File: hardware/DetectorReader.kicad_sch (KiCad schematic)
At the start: 17 parts, among them J1 10118194-0001LF, J2 Combo_Conn, J4 SMA_Conn, SW1 SeqTrig_SW, U1 ATtiny814-SS, U2 FT231XS-R, U3 XC0900P-10S

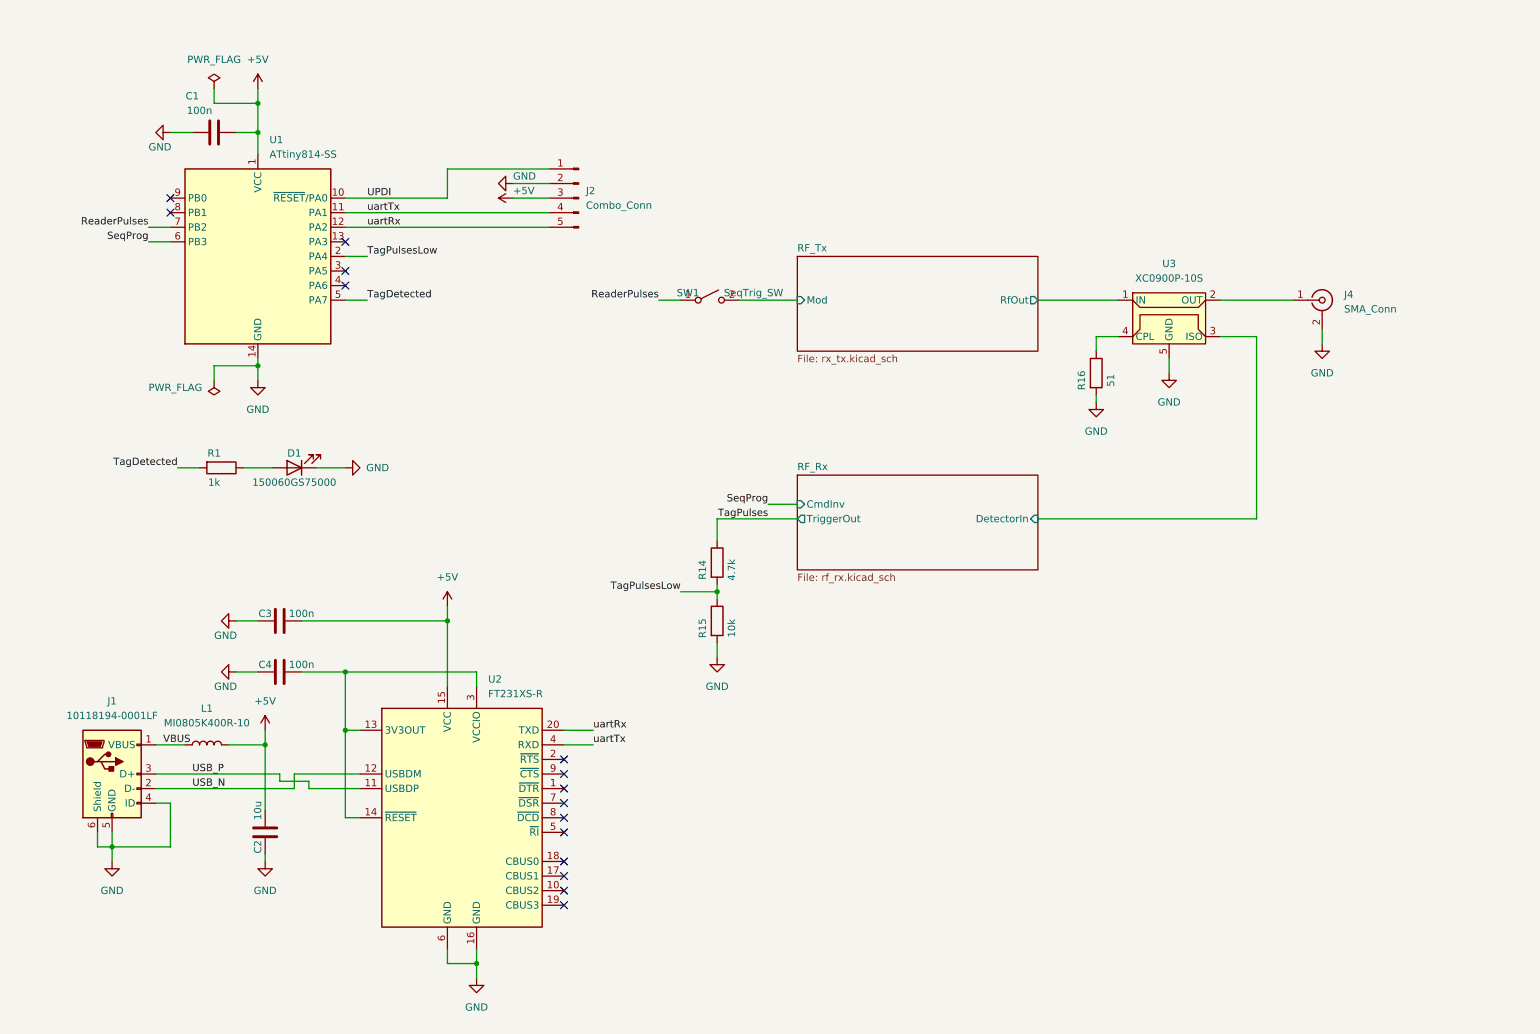
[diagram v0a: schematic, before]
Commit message: splitted quad opamp into dual opamp and comparator for better digitalization and smaller board
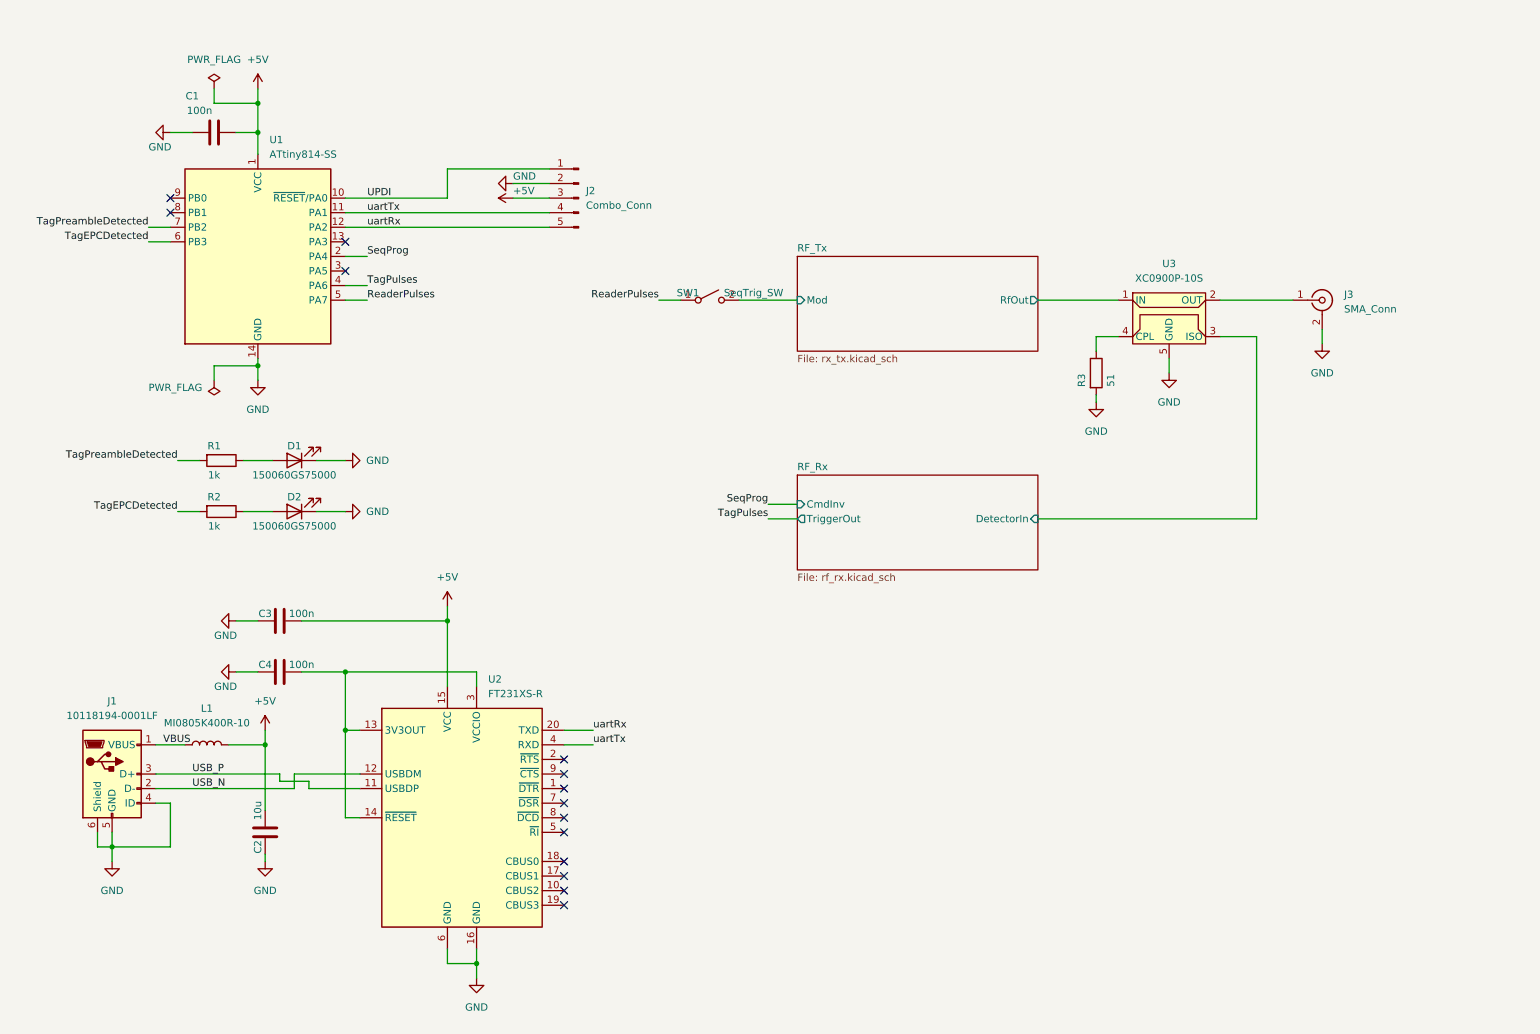
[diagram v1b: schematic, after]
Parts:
- removed R14: 4.7k, Resistor_SMD:R_0603_1608Metric, symbol Device:R
- removed R15: 10k, Resistor_SMD:R_0603_1608Metric, symbol Device:R
- added D1: 150060GS75000, LED_SMD:LED_0603_1608Metric, symbol Device:LED
- added R1: 1k, Resistor_SMD:R_0603_1608Metric, symbol Device:R
- renumbered D1 to D2, J4 to J3, R1 to R2, R16 to R3
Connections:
- net TagPulsesLow is gone; now on net SeqProg: U1.2 (PA4)
- net GND: now also D1.1 (K)
- net ReaderPulses: now also U1.5 (PA7); no longer U1.7 (PB2)
- net SeqProg: no longer U1.6 (PB3)
- net TagPulses: now also U1.4 (PA6)
- net TagDetected renamed TagEPCDetected
- net TagEPCDetected: now also U1.6 (PB3); no longer U1.5 (PA7)
- new net: D1.2 (A), R1.1
- new net TagPreambleDetected: R1.2, U1.7 (PB2)
- no-connect marks 15 -> 14
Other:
- moved on the sheet: D2, R2

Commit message: Updated schematic, PCB and fabrication files
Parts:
- added C3, C6, C7: 22u, Capacitor_SMD:C_0603_1608Metric, symbol Device:C
- added L2, L3: MI0805K400R-10, Inductor_SMD:L_0805_2012Metric, symbol Device:L
- C2: value 10u -> 22u
- D1: value 150060GS75000 -> 150060RS75000
- renumbered C3 to C4, C4 to C5
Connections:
- net +5V: now also C3.2, L2.1, L3.1; no longer C1.2, U1.1 (VCC)
- net GND: now also C3.1, C6.1, C7.1
- new net +5VAnalog: C7.2, L3.2
- new net +5VDigital: C1.2, C6.2, L2.2, U1.1 (VCC)
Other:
- moved on the sheet: C2, C4, C5, U2

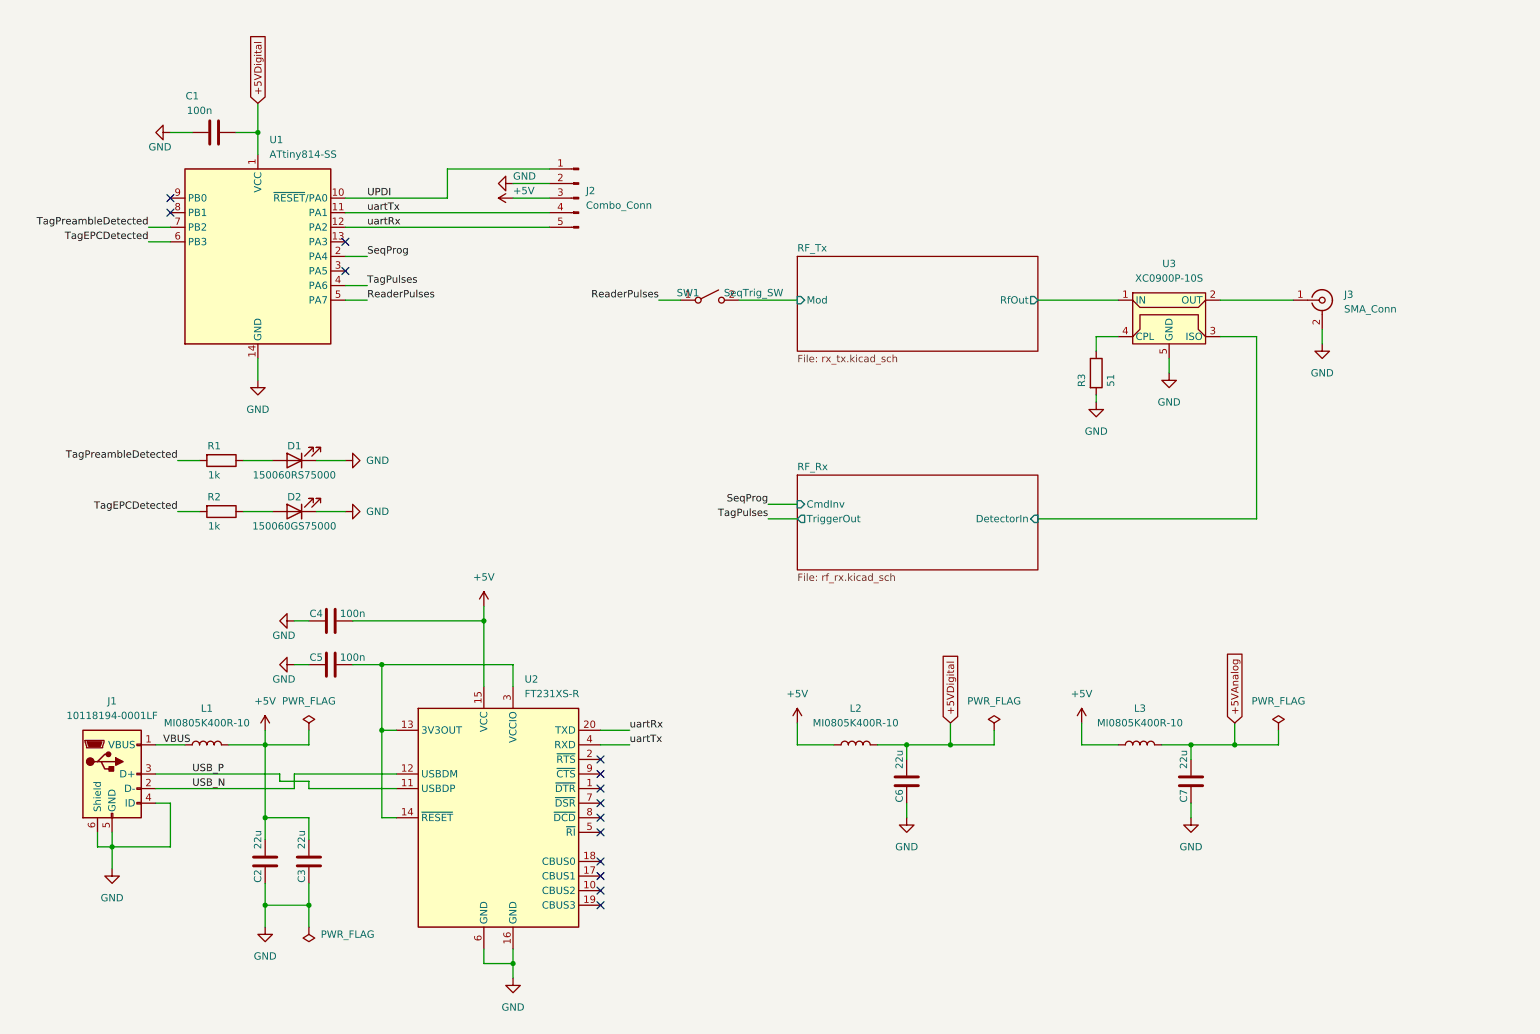
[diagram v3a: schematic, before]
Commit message: Rev 2. Using USB-C, configurable Tx, op-amp based LF amplifier, tri-color indicator. Using platformIO for firmware, splitted code into separate files.
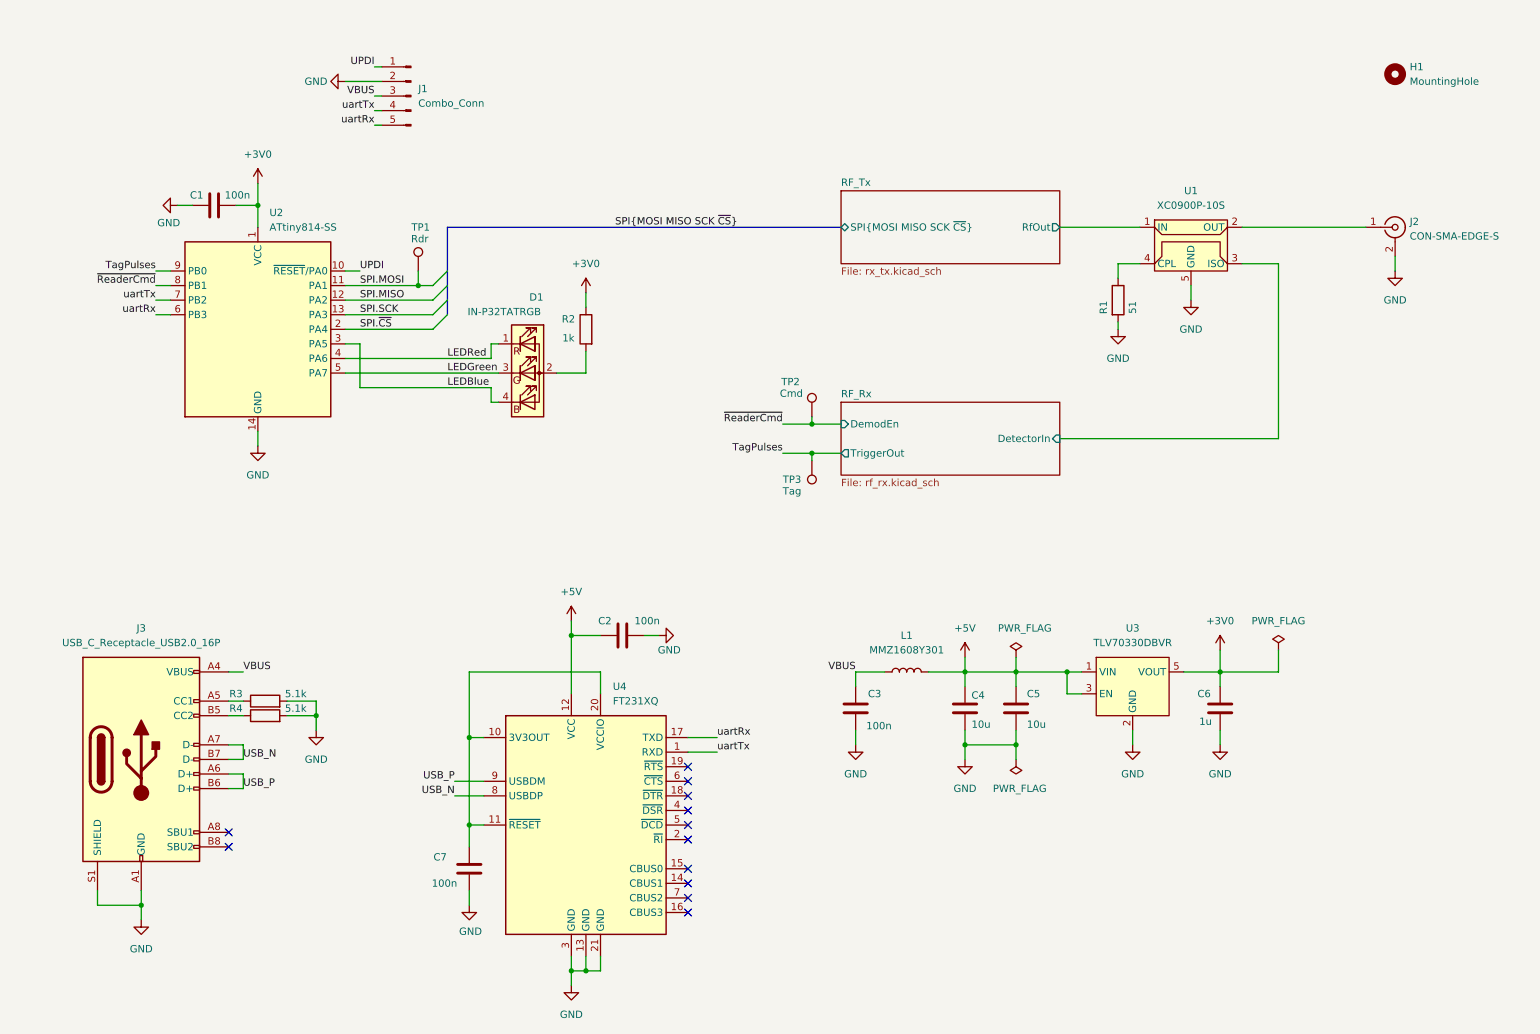
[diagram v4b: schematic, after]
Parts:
- removed C7: 22u, Capacitor_SMD:C_0603_1608Metric, symbol Device:C
- removed D1: 150060RS75000, LED_SMD:LED_0603_1608Metric, symbol Device:LED
- removed D2: 150060GS75000, LED_SMD:LED_0603_1608Metric, symbol Device:LED
- removed J1: 10118194-0001LF, Connector_USB:USB_Micro-B_Amphenol_10118194_Horizontal, symbol Connector:USB_B_Micro
- removed J2: Combo_Conn, Connector_PinHeader_2.54mm:PinHeader_1x05_P2.54mm_Vertical, symbol Connector:Conn_01x05_Male
- removed L2, L3: MI0805K400R-10, Inductor_SMD:L_0805_2012Metric, symbol Device:L
- removed R2: 1k, Resistor_SMD:R_0603_1608Metric, symbol Device:R
- removed SW1: SeqTrig_SW, Connector_PinHeader_2.54mm:PinHeader_1x02_P2.54mm_Vertical, symbol Switch:SW_SPST
- removed U2: FT231XS-R, Package_SO:SSOP-20_3.9x8.7mm_P0.635mm, symbol Interface_USB:FT231XS
- added C3: 100n, Capacitor_SMD:C_0603_1608Metric, symbol Device:C
- added D1: IN-P32TATRGB, ProjLib:LED_SMD_IN-P32TATRGB, symbol Device:LED_RAGB
- added H1: MountingHole, MountingHole:MountingHole_3.2mm_M3_DIN965, symbol Mechanical:MountingHole
- added J1: Combo_Conn, Connector_PinHeader_2.54mm:PinHeader_1x05_P2.54mm_Vertical, symbol Connector:Conn_01x05_Pin
- added J3: USB_C_Receptacle_USB2.0_16P, Connector_USB:USB_C_Receptacle_GCT_USB4105-xx-A_16P_TopMnt_Horizontal, symbol Connector:USB_C_Receptacle_USB2.0_16P
- added R3, R4: 5.1k, Resistor_SMD:R_0603_1608Metric, symbol Device:R
- added TP1: Rdr, ProjLib:Single_Pin, symbol Connector:TestPoint
- added TP2: Cmd, ProjLib:Single_Pin, symbol Connector:TestPoint
- added TP3: Tag, ProjLib:Single_Pin, symbol Connector:TestPoint
- added U3: TLV70330DBVR, Package_TO_SOT_SMD:SOT-23-5, symbol ProjLib:TLV70330
- added U4: FT231XQ, Package_DFN_QFN:QFN-20-1EP_4x4mm_P0.5mm_EP2.5x2.5mm, symbol Interface_USB:FT231XQ
- C4: renamed from C2; value 22u -> 10u
- C5: renamed from C3; value 22u -> 10u
- C6: value 22u -> 1u
- J2: renamed from J3; value SMA_Conn -> CON-SMA-EDGE-S; footprint Connector_Coaxial:SMA_Samtec_SMA-J-P-X-ST-EM1_EdgeMount -> Connector_Coaxial:SMA_Samtec_SMA-J-P-H-ST-EM1_EdgeMount
- L1: value MI0805K400R-10 -> MMZ1608Y301; footprint Inductor_SMD:L_0805_2012Metric -> Inductor_SMD:L_0603_1608Metric
- renumbered C4 to C2, C5 to C7, R3 to R1, R1 to R2, U3 to U1, U1 to U2
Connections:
- net +5VDigital is gone; now on net +3V0: C1.2, C6.2, U2.1 (VCC)
- net TagEPCDetected is gone; now on net uartRx: U2.6 (PB3)
- net +5V: now also U3.1 (VIN), U3.3 (EN), U4.12 (VCC)
- net GND: now also C3.1, J1.2 (Pin_2), J3.A1 (GND), J3.A12 (GND), J3.B1 (GND), J3.B12 (GND), J3.S1 (SHIELD), R3.2, R4.2, U3.2 (GND), U4.13 (GND), U4.21 (GND), U4.3 (GND)
- net TagPulses: now also U2.9 (PB0), TP3.1; no longer U2.4 (PA6)
- net UPDI: now also J1.1 (Pin_1)
- net USB_N: now also J3.A7 (D-), J3.B7 (D-), U4.8 (USBDP)
- net USB_P: now also J3.A6 (D+), J3.B6 (D+), U4.9 (USBDM)
- net VBUS: now also C3.2, J1.3 (Pin_3), J3.A4 (VBUS), J3.A9 (VBUS), J3.B4 (VBUS), J3.B9 (VBUS)
- net uartRx: now also J1.5 (Pin_5), U4.17 (TXD); no longer U2.12 (PA2)
- net uartTx: now also U2.7 (PB2), J1.4 (Pin_4), U4.1 (RXD); no longer U2.11 (PA1)
- net at C7.2: now also U4.10 (3V3OUT), U4.11 (~{RESET}), U4.20 (VCCIO)
- net +3V0: now reaches R2.1
- net +3V0: now also U3.5 (VOUT)
- net SPI.SCK: now reaches U2.13 (PA3)
- net LEDBlue: now reaches U2.3 (PA5)
- net LEDBlue: now also D1.4 (BK)
- net ~{ReaderCmd}: now reaches U2.8 (PB1)
- net ~{ReaderCmd}: now also TP2.1
- net ReaderPulses renamed LEDGreen
- net LEDGreen: now also D1.3 (GK)
- net SeqProg renamed SPI.~{CS}
- net TagPreambleDetected: no longer names the net of R2.2
- net TagPreambleDetected: now also D1.2 (A); no longer U2.7 (PB2)
- new net: J3.A5 (CC1), R3.1
- new net: J3.B5 (CC2), R4.1
- new net LEDRed: D1.1 (RK), U2.4 (PA6)
- new net SPI.MISO: U2.12 (PA2)
- new net SPI.MOSI: TP1.1, U2.11 (PA1)
- no-connect marks 14 -> 12
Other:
- sheet RF_Rx ports: added DemodEn; removed CmdInv
- sheet RF_Tx ports: added SPI{MOSI MISO SCK ~{CS}}; removed Mod
- moved on the sheet: C1, C2, C4, C5, C7, J2, L1, R1, R2, U1, U2

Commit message: Rev 3. Back to transistor-based design since op-amp approach did not work well. Using UART bridge from other brand as FTDI was sold out.
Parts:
- removed C3, C7: 100n, Capacitor_SMD:C_0603_1608Metric, symbol Device:C
- removed L1: MMZ1608Y301, Inductor_SMD:L_0603_1608Metric, symbol Device:L
- removed U4: FT231XQ, Package_DFN_QFN:QFN-20-1EP_4x4mm_P0.5mm_EP2.5x2.5mm, symbol Interface_USB:FT231XQ
- added C6: 1u, Capacitor_SMD:C_0603_1608Metric, symbol Device:C
- added U4: CY7C65211-24LTXI, Package_DFN_QFN:QFN-24-1EP_4x4mm_P0.5mm_EP2.6x2.6mm, symbol Interface_USB:CY7C65211-24LTXI
- C5: renamed from C6; value 1u -> 10u
- R1: value 51 -> 50
- renumbered C4 to C3, C5 to C4
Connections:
- net +5V: now also J1.2 (Pin_2), J3.A4 (VBUS), J3.A9 (VBUS), J3.B4 (VBUS), J3.B9 (VBUS), U4.15 (VBUS), U4.24 (VDDD)
- net GND: now also J1.3 (Pin_3), C6.1, U4.13 (VSSD), U4.16 (VSSD), U4.17 (VSSA), U4.3 (VSSD); no longer J1.2 (Pin_2)
- net USB_N: now also U4.11 (USBDM)
- net USB_P: now also U4.10 (USBDP)
- net uartRx: now also U4.23 (SCB_4/GPIO_5)
- net uartTx: now also U4.1 (SCB_0/GPIO_6)
- removed net VBUS: J1.3 (Pin_3), J3.A4 (VBUS), J3.A9 (VBUS), J3.B4 (VBUS), J3.B9 (VBUS)
- new net: C6.2, U4.12 (VCCD)
- no-connect marks 12 -> 15
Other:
- moved on the sheet: C2, H1, J2
